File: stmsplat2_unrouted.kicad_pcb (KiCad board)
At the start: 2 copper layers, 100 x 100 mm, 113 parts, among them J1 C11_2X36, J10 Conn_01x03_Male, J11 Conn_01x02_Male, J12 Conn_01x04_Male, J13 Conn_01x04_Male, J14 Conn_01x02, J15 Conn_01x02, J16 Screw_Terminal_01x03, J17 Screw_Terminal_01x02, J2 C12_2X36, J3 Conn_01x04_Male, J4 Conn_01x04_Male, J5 Conn_Coaxial, J6 Conn_01x04_Male, J7 Conn_01x04_Male, J8 Conn_01x04_Male, J9 Conn_01x03_Male, Q1 BSS138LT1G, U1 ublox_chinese_PCB_module, U10 XCVR_E30-400M20S (Si4463), U11 3115_module, U2 ESP-C3-13U, U3 SST25VF032B, U4 48L512-48LM01, U5 Opamp_Quad_MCP6024, U6 E180-ZG120A, U7 AZ1084C, U8 MCP6S93-X_UN, U9 DS2485

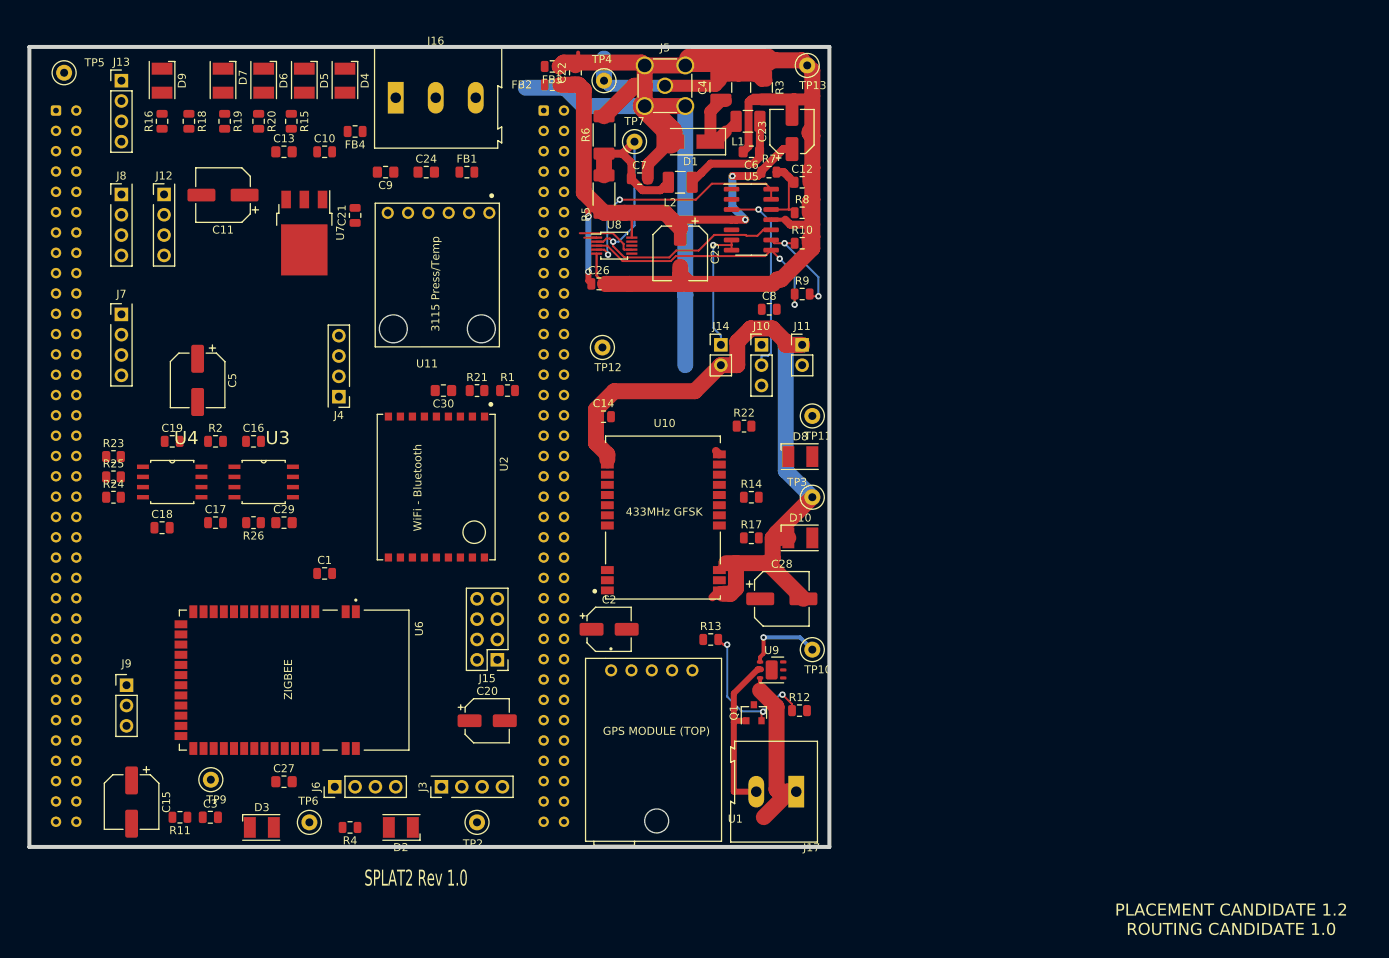
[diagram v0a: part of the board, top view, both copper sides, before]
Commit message: placement candidate 2 with routed candidate 1.0
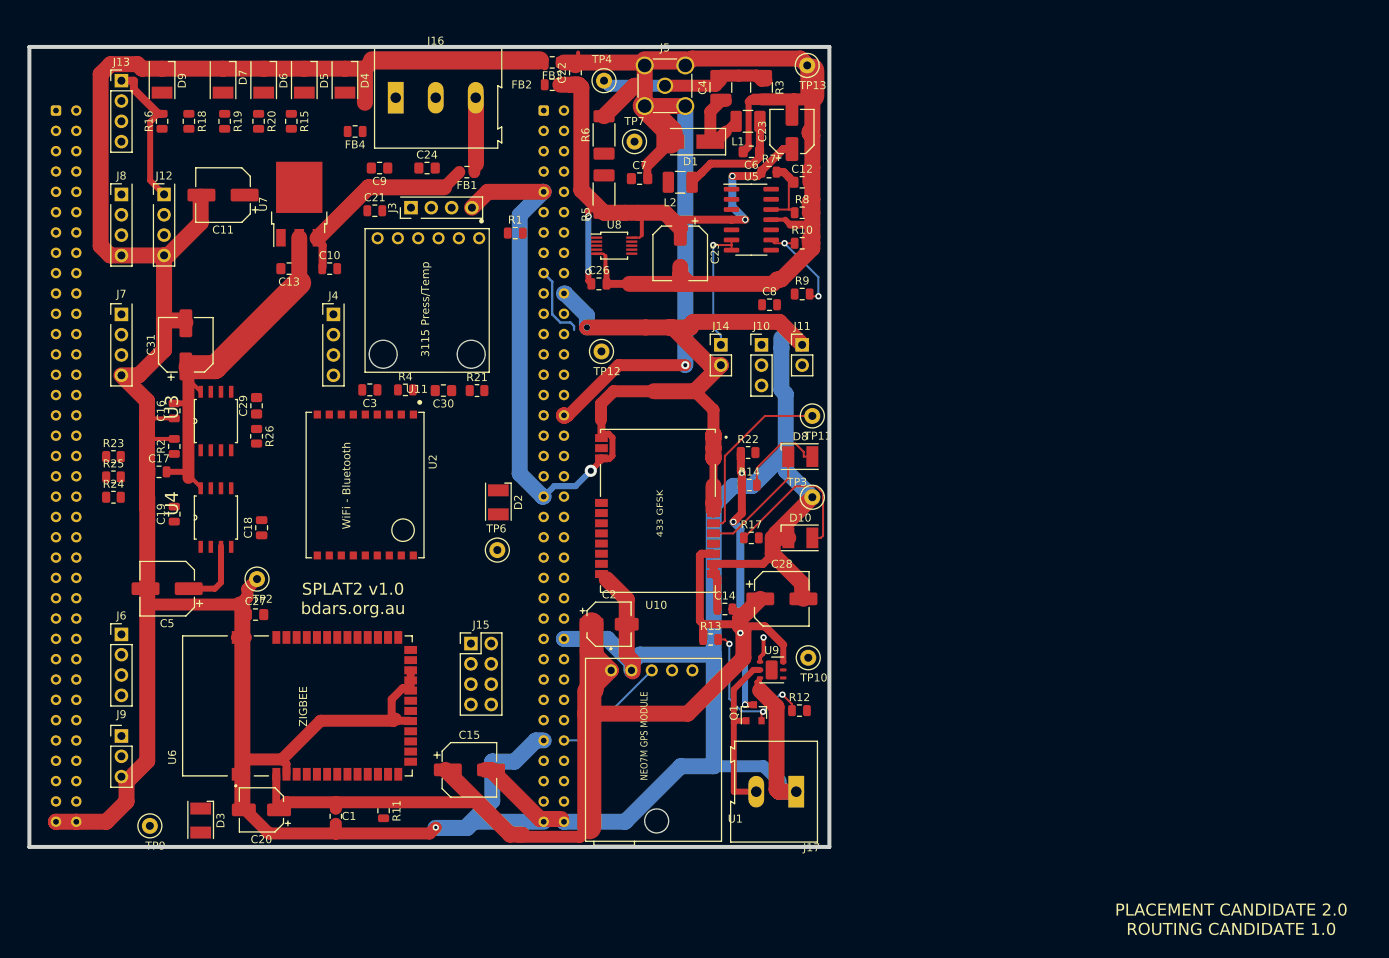
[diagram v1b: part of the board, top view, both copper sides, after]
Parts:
- removed TP5: TestPoint, TestPoint:TestPoint_Loop_D1.80mm_Drill1.0mm_Beaded
- added C31: 100uF, Capacitor_SMD:CP_Elec_6.3x7.7, F.Cu at (71.5, 102.9)
- U10: footprint XCVR_E30-400M20S -> splat2footprints:XCVR_E30-400M20S
- moved J3 72.5 mm to (99.7, 85.7)
- moved C3 57.0 mm to (94.5, 108.5), turned to 180 degrees
- moved R4 55.1 mm to (99.0, 108.5), turned to 0 degrees
- moved D2 42.4 mm to (110.6, 122.6), turned to 270 degrees
- moved C15 42.4 mm to (107.0, 156.0), turned to 0 degrees
- moved TP6 41.4 mm to (110.5, 128.5)
- moved TP2 41.0 mm to (80.5, 132.2)
- moved J6 32.8 mm to (63.5, 139.1), turned to 0 degrees
- moved C1 30.4 mm to (90.3, 161.8), turned to 270 degrees
- moved C20 30.3 mm to (81.0, 161.0), turned to 180 degrees
- moved C14 28.4 mm to (138.9, 135.9)
- moved C5 26.3 mm to (69.2, 133.3), turned to 180 degrees
- moved R11 25.5 mm to (96.3, 161.1), turned to 270 degrees
- moved C27 21.2 mm to (80.3, 136.6)
- moved R1 19.7 mm to (112.7, 88.9)
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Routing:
- net GND: track 117.1 -> 684.5 mm, vias 0 -> 3
- net VDD: track 0.00 -> 248.0 mm, vias 0 -> 4
- net Net-(C7-Pad1): track 56.1 -> 0.00 mm, vias 1 -> 0
- net Net-(R9-Pad1): track 32.5 -> 0.00 mm, vias 2 -> 0
- net /HALF3V3: track 30.7 -> 0.00 mm, vias 2 -> 0
- net +5V: track 0.00 -> 25.1 mm
- net Net-(J10-Pad2): track 24.4 -> 0.00 mm, vias 1 -> 0
- net Net-(TP11-Pad1): track 0.00 -> 22.7 mm
- net Net-(D10-Pad2): track 0.00 -> 19.7 mm
- net Net-(D8-Pad1): track 0.00 -> 14.9 mm
- net PE0: track 0.00 -> 14.6 mm
- net Net-(D8-Pad2): track 0.00 -> 12.4 mm
- net PB6: track 0.00 -> 9.41 mm
- net /RAW5V: track 0.00 -> 9.36 mm
- net Net-(C5-Pad1): track 0.00 -> 8.92 mm
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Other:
- board text added: "433 GFSK"
- board text added: "PLACEMENT CANDIDATE 2.0 ROUTING CANDIDATE 1.0"
- board text added: "SPLAT2 v1.0 bdars.org.au"
- board text removed: "PLACEMENT CANDIDATE 1.2 ROUTING CANDIDATE 1.0"
- board text removed: "SPLAT2 Rev 1.0"
